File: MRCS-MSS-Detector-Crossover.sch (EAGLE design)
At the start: 11 parts, among them J1 RJ45, J2 RJ45, X1 TRACK, X2 AUXBUS, X3 BLK OCC, X4 0.156/5

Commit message: fix commas in xml
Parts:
- C1, C2: device cap-pan:E2,5-6 -> cap-pan:E2.5-6
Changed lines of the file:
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@@
 <part name="X3" library="con-phoenix-350" deviceset="1751248" device="" value="BLK OCC"/>
 <part name="BR1" library="rectifier" deviceset="RB1A" device="" value="bridge"/>
-<part name="C1" library="cap-pan" deviceset="E2,5-6" device="" value="47uf 25V"/>
-<part name="C2" library="cap-pan" deviceset="E2,5-6" device="" value="0.47uf 63V"/>
+<part name="C1" library="cap-pan" deviceset="E2.5-6" device="" value="47uf 25V"/>
+<part name="C2" library="cap-pan" deviceset="E2.5-6" device="" value="0.47uf 63V"/>
 <part name="X4" library="con-molex" deviceset="KK-156-5" device="" value="0.156/5"/>
 <part name="VR1" library="v-reg" deviceset="78LXX" device="" value="LM78L12"/>

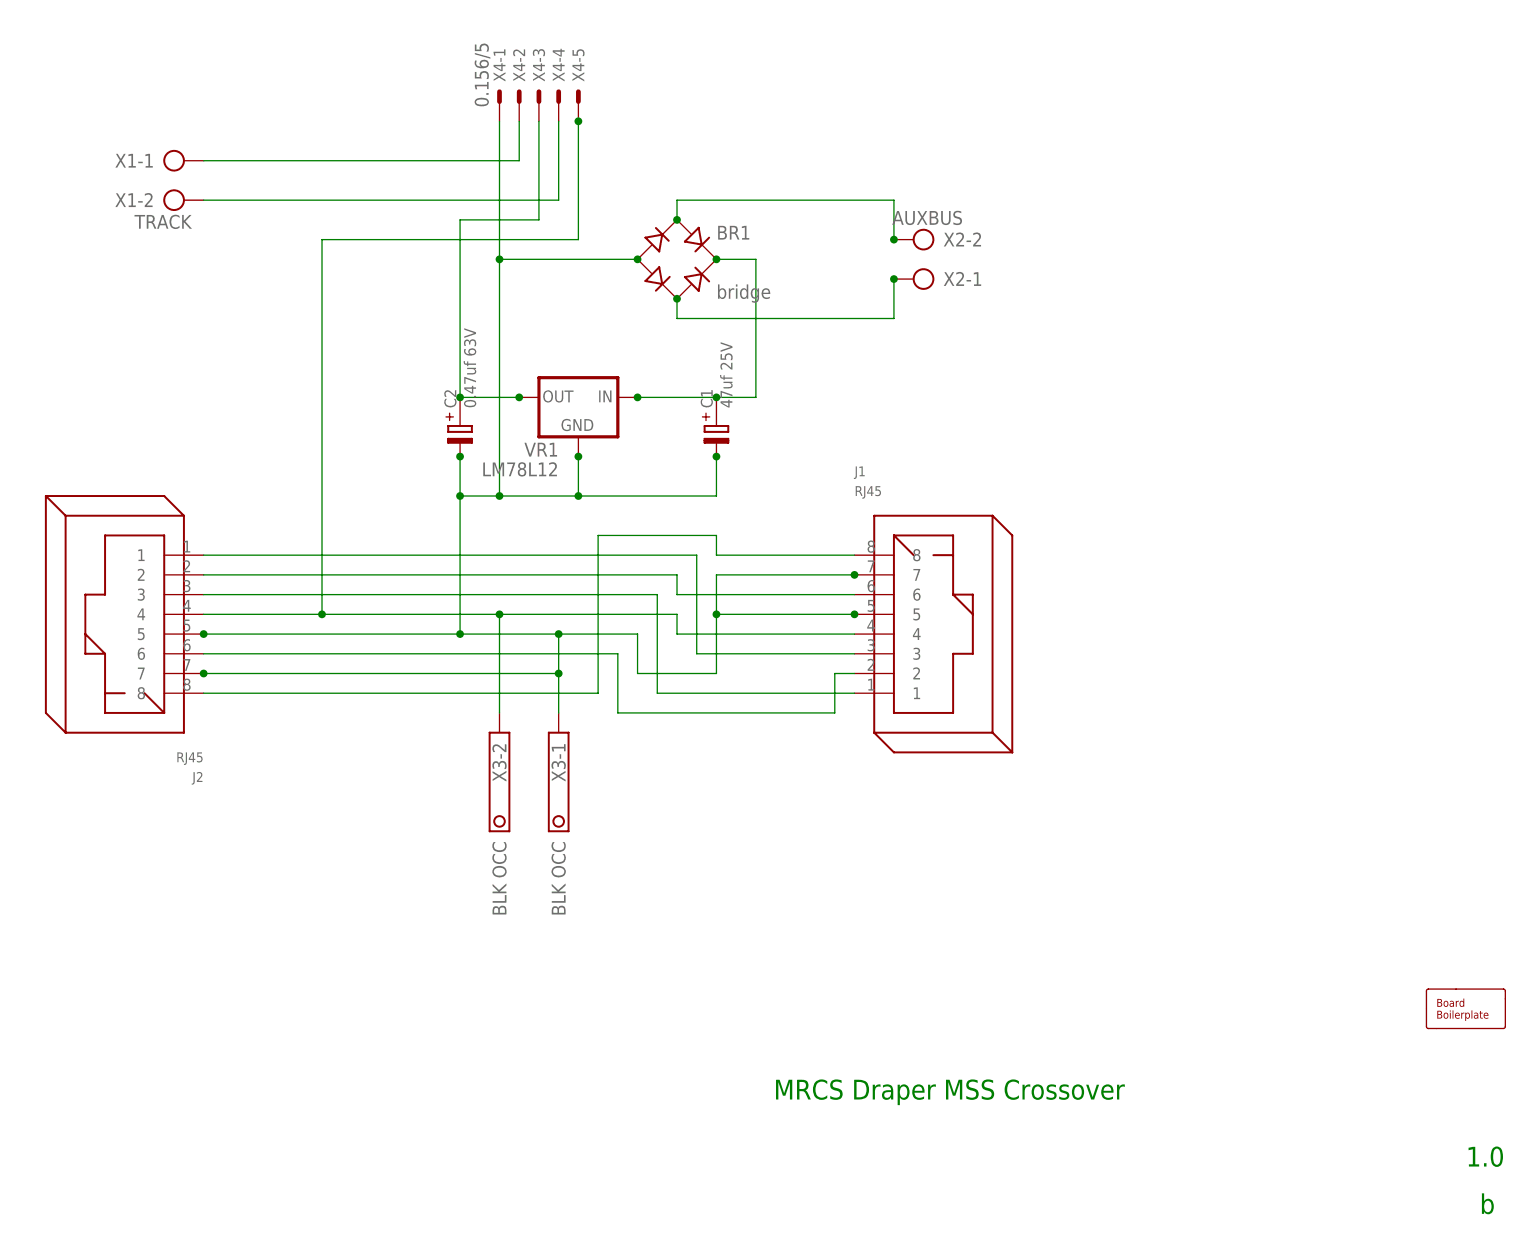
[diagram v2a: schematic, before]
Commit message: Moved all components into SPCoast.lbr and panelized
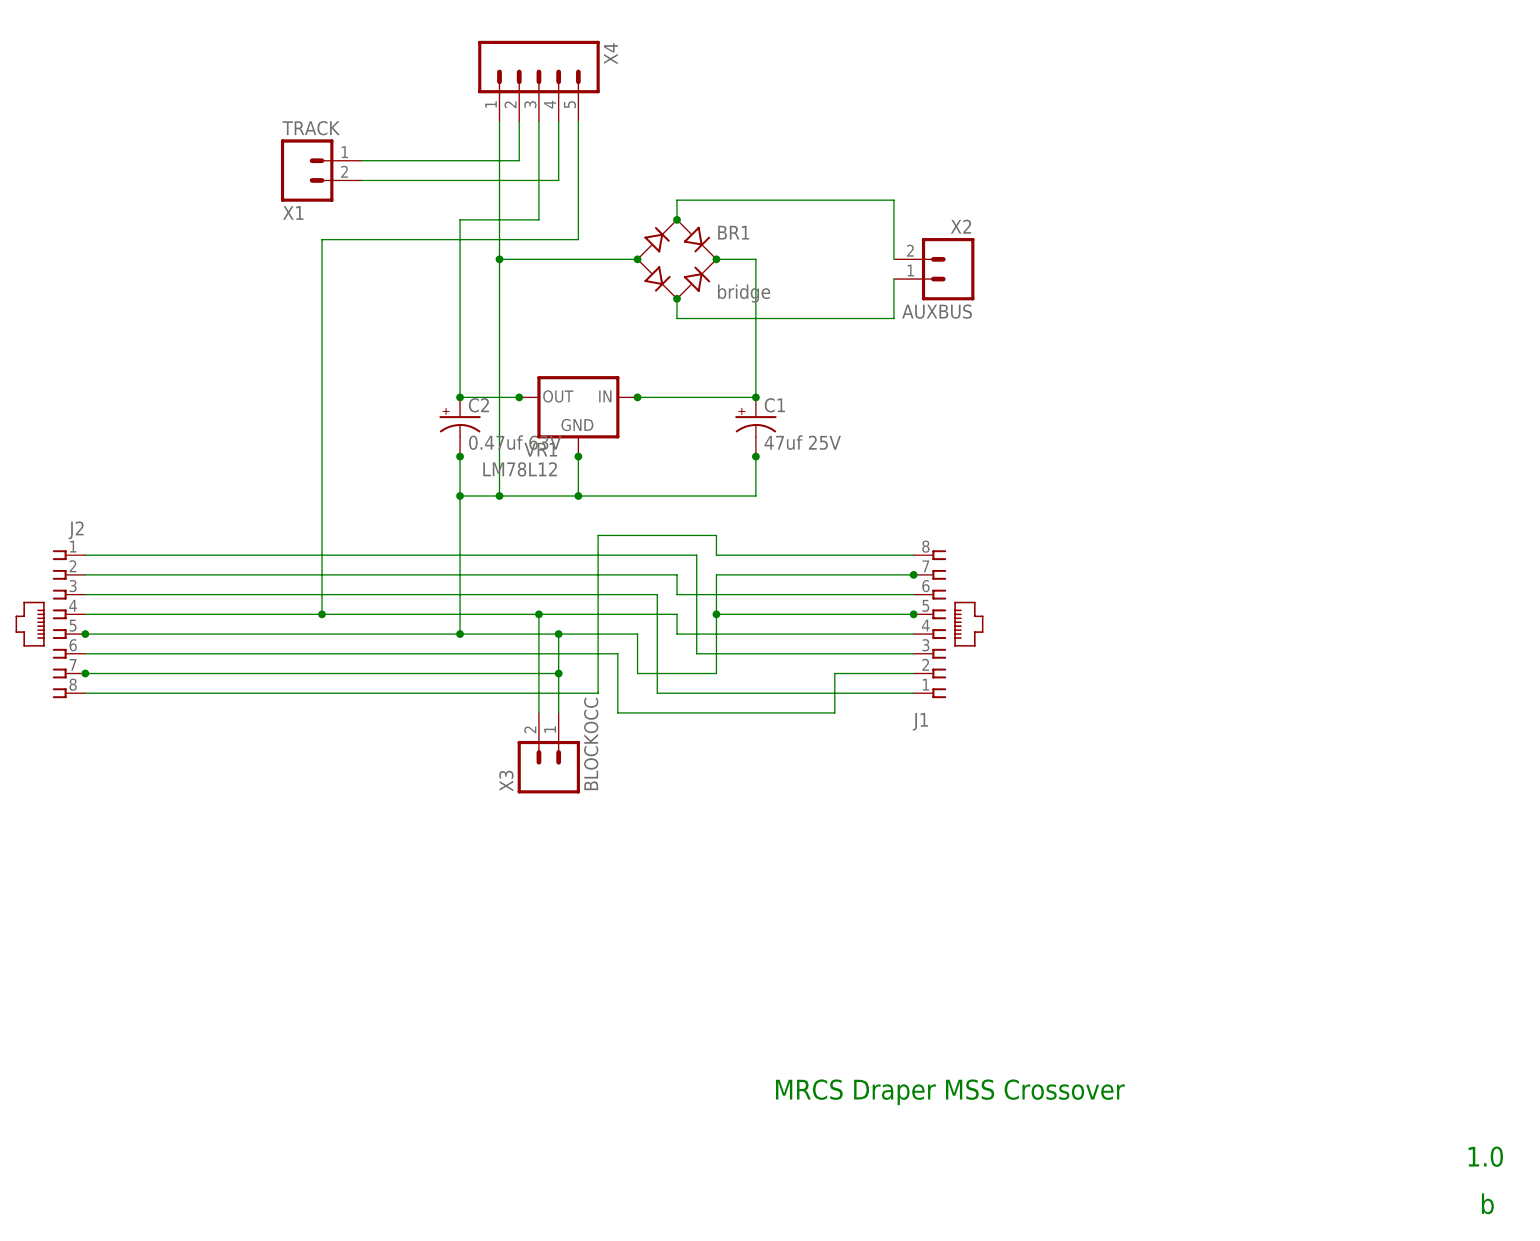
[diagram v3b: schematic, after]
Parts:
- removed BOARD1: SEEED Fusion, SPCoast:BOARD50X50-NOHOLES
- BR1: device rectifier:RB1A -> SPCoast:DBRB1AG
- C1, C2: device cap-pan:E2.5-6 -> SPCoast:CAP-POLPTH-2.5MM
- J1, J2: value RJ45 -> (none); device con-rj:RJ45 -> SPCoast:CONNECTOR-RJ45-FRONT
- VR1: device v-reg:78LXX -> SPCoast:VREG-TO-92-12
- X1, X2: device con-ptr500:AK500/2 -> SPCoast:CONNECTOR-M025MM-LOCK
- X3: value BLK OCC -> BLOCKOCC; device con-phoenix-350:1751248 -> SPCoast:CONNECTOR-M025MM-LOCK
- X4: value 0.156/5 -> (none); device con-molex:KK-156-5 -> SPCoast:CONNECTOR-M051.56
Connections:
- net AC1: now also X2.B; no longer X2-2.KL
- net AC2: now also X2.A; no longer X2-1.KL
- net GND: now also X3.A, X4.1; no longer X3-1.K, X4-1.S
- net N$10: now also X3.B, X4.5; no longer X3-2.K, X4-5.S
- net TRACK1: now also X1.A, X4.2; no longer X1-1.KL, X4-2.S
- net TRACK2: now also X1.B, X4.4; no longer X1-2.KL, X4-4.S
- net V12: now also X4.3; no longer X4-3.S
